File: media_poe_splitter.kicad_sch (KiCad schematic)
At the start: 30 parts, among them J1 Screw_Terminal_01x02, X1 7499811120

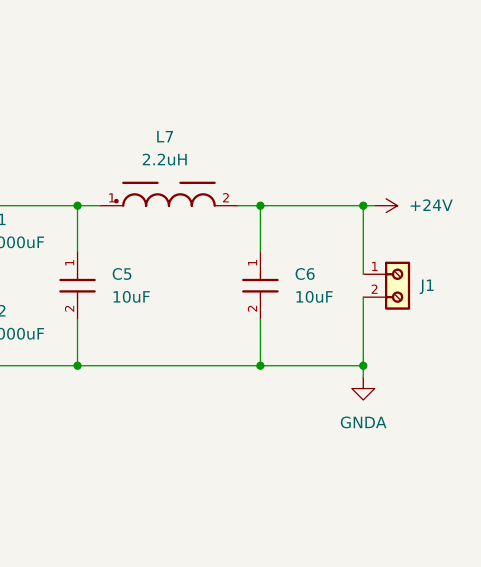
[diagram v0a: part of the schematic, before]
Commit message: poe: add missing tracks
Signed-off-by: Marc 'risson' Schmitt <marc.schmitt@risson.space>
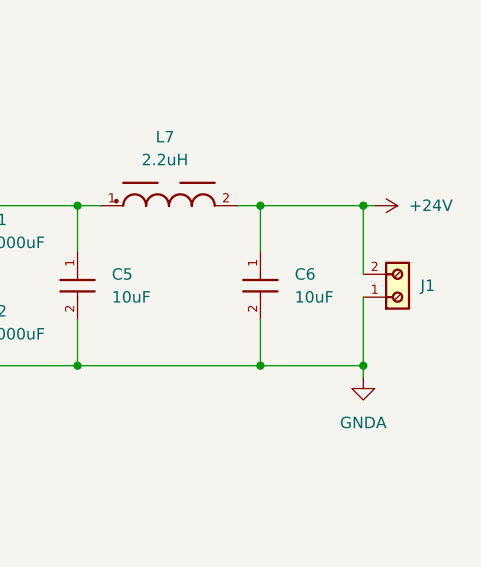
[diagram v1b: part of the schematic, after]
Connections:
- net +24V: now also J1.2; no longer J1.1
- net GNDA: now also J1.1; no longer J1.2
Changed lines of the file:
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@@
 	(symbol
 		(lib_id "691210910002:691210910002")
-		(at 415.29 382.27 270)
+		(at 415.29 379.73 270)
+		(mirror x)
 		(unit 1)
 		(exclude_from_sim no)
@@
 		(on_board yes)
 		(dnp no)
-		(fields_autoplaced yes)
 		(property "Reference" "J1"
-			(at 416.56 380.9999 90)
+			(at 416.56 381.0001 90)
 			(effects
 				(font
@@
 		)
 		(property "Value" "Screw_Terminal_01x02"
-			(at 412.7501 384.81 0)
+			(at 412.7501 377.19 0)
 			(effects
 				(font
@@
 		)
 		(property "Footprint" "691210910002:691210910002"
-			(at 415.29 382.27 0)
+			(at 415.29 379.73 0)
 			(effects
 				(font
@@
 		)
 		(property "Datasheet" "https://www.we-online.com/components/products/datasheet/691210910002.pdf"
-			(at 415.29 382.27 0)
+			(at 415.29 379.73 0)
 			(effects
 				(font
@@
 		)
 		(property "Description" "WR-TBL Series 2109 - Rising Cage Clamp - THT - 2.54mm"
-			(at 415.29 382.27 0)
+			(at 415.29 379.73 0)
 			(effects
 				(font
@@
 		)
 		(property "Mount" "THT"
-			(at 415.29 382.27 0)
+			(at 415.29 379.73 0)
 			(effects
 				(font
@@
 		)
 		(property "MPN" "691210910002"
-			(at 415.29 382.27 0)
+			(at 415.29 379.73 0)
 			(effects
 				(font
@@
 		)
 		(property "Manufacturer" "Wurth Elektronik"
-			(at 415.29 382.27 0)
+			(at 415.29 379.73 0)
 			(effects
 				(font
@@
 		)
 		(property "Manufactuer" ""
-			(at 415.29 382.27 0)
+			(at 415.29 379.73 0)
 			(effects
 				(font

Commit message: add USB controller, finish board
Signed-off-by: Marc 'risson' Schmitt <marc.schmitt@risson.space>
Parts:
- removed C5, C6: 10uF, 885012209073:885012209073, symbol 885012209073:885012209073
- removed L7: 2.2uH, 744774022:744774022, symbol 744774022:744774022
- added C10, C11, C12, C13, C18, C20, C23, C24, C25, C26, C27, C28, C29, C30, C31, C32, C5, C6, C7: 100nF 25V, 885012206071:885012206071, symbol 885012206071:885012206071
- added C14, C15, C19: 1uF 16V, 885012206052:885012206052, symbol 885012206052:885012206052
- added C16, C3: 15pF 50V, 885012005056:885012005056, symbol 885012005056:885012005056
- added C17, C33: 10uF 6.3V, 885012207003:885012207003, symbol 885012207003:885012207003
- added C4: 2.2uF 25V, 885012207079:885012207079, symbol 885012207079:885012207079
- added C8: 10nF 6.3V, 885012104004:885012104004, symbol 885012104004:885012104004
- added D10, D11: 5Vdc, 824014885:824014885, symbol 824014885:824014885
- added D13: 824012823, 824012823:824012823, symbol 824012823:824012823
- added IC1: LAN7850-I_8JX, LAN7850-I_8JX:LAN7850-I_8JX, symbol LAN7850-I_8JX:LAN7850-I_8JX
- added IC2: 17791063215, 17791063215:17791063215, symbol 17791063215:17791063215
- added IC3: 93AA66C-I/SN, 93AA66C-I_SN:93AA66C-I_SN, symbol 93AA66C-I_SN:93AA66C-I_SN
- added L7: 744232090, 744232090:744232090, symbol 744232090:744232090
- added L9: VLF302515MT-3R3M, VLF302515MT-3R3M:VLF302515MT-3R3M, symbol VLF302515MT-3R3M:VLF302515MT-3R3M
- added R1, R3, R4, R7: 10K, RC0603FR-0710KL:RC0603FR-0710KL, symbol RC0603FR-0710KL:RC0603FR-0710KL
- added R10: 12K, RC0603FR-0712KL:RC0603FR-0712KL, symbol RC0603FR-0712KL:RC0603FR-0712KL
- added R11, R2: 330R, RC0603FR-07340RL:RC0603FR-07340RL, symbol RC0603FR-07340RL:RC0603FR-07340RL
- added R6: 47.8K, RC0603FR-0748K7L:RC0603FR-0748K7L, symbol RC0603FR-0748K7L:RC0603FR-0748K7L
- added R8: 2K, RC0603FR-072KL:RC0603FR-072KL, symbol RC0603FR-072KL:RC0603FR-072KL
- added R9: 100K, RC0603FR-07100KL:RC0603FR-07100KL, symbol RC0603FR-07100KL:RC0603FR-07100KL
- added S1: 435151014824, 435151014824:435151014824, symbol 435151014824:435151014824
- added X2: 68710614522, 68710614522:68710614522, symbol 68710614522:68710614522
- added Y1: 830055299, 830055299:830055299, symbol 830055299:830055299
- C101, C21, C22, D1, D2, D3, D4, D5, D6, D7, D8, D9, R101, R102, R103, R104: Mount SMD -> SMT
- L1, L2, L3, L4, L5, L6: Manufacturer Wurth Electronics -> Wurth Elektronik; Mount SMD -> SMT
- X1: Manufacturer Würth Elektronik -> Wurth Elektronik
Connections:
- net +24V: now also B1.10 (VOUT2), B1.9 (VOUT2), C1.1, C4.1, C7.1, IC2.2 (+VIN)
- net GNDA: now also C4.2, C7.2, IC2.1 (-VIN)
- net GNDPWR: now also C13.2, C6.2, R11.2, R2.2, S1.5, S1.6, X2.6, X2.Z1, X2.Z2
- net TR3_P: now reaches X1.11 (TRD4+)
- net TR3_P: now also D11.6, IC1.10 (TR3P)
- net TR3_N: now reaches X1.12 (TRD4-)
- net TR3_N: now also D11.5, IC1.11 (TR3N)
- net TR1_P: now reaches X1.2 (TRD2+)
- net TR1_P: now also D10.6, IC1.4 (TR1P)
- net TR1_N: now reaches X1.3 (TRD2-)
- net TR1_N: now also D10.5, IC1.5 (TR1N)
- net TR2_P: now reaches X1.4 (TRD3+)
- net TR2_P: now also D11.1, IC1.7 (TR2P)
- net TR2_N: now reaches X1.5 (TRD3-)
- net TR2_N: now also D11.9, IC1.8 (TR2N)
- net TR0_P: now reaches X1.7 (TRD1+)
- net TR0_P: now also D10.1, IC1.1 (TR0P)
- net TR0_N: now reaches X1.8 (TRD1-)
- net TR0_N: now also D10.9, IC1.2 (TR0N)
- new net: IC1.18 (VDD12_SW_OUT), L9.1
- new net: C3.1, IC1.46 (XI), Y1.1
- new net: C16.1, IC1.47 (XO), Y1.3
- new net: IC1.21 (EECS/GPIO1), IC3.1 (CS), R7.1
- new net: IC1.22 (EEDI/GPIO2), IC3.3 (DI)
- new net: IC1.23 (EEDO/GPIO3), IC3.4 (DO)
- new net: IC1.24 (EECLK/GPIO4), IC3.2 (CLK)
- new net: IC1.27 (VBUS_DET), R4.1
- new net: IC1.40 (TEST), R1.1
- new net: IC1.43 (USBRBIAS), R10.1
- new net: IC1.55 (REF_REXT), R8.1
- new net: C19.2, IC1.56 (REF_FILT)
- new net: IC3.6 (ORG), R3.1
- new net: D13.2, L7.1, X2.3
- new net: D13.1, L7.4, X2.2
- new net: IC2.8 (FB), R6.1
- new net +1V2: C11.2, C12.1, C17.1, C18.1, C20.1, C23.1, C24.1, IC1.20 (VDD12_SW_FB), IC1.26 (VDD12CORE), IC1.33 (VDD12A), IC1.34 (VDD12HSIC), IC1.48 (VDD12CORE), IC1.52 (VDD12A), L9.2
- new net +2V5: C14.1, C25.1, C26.1, C27.1, C28.1, IC1.12 (VDD25A), IC1.3 (VDD25A), IC1.53 (VDD25_REG_OUT), IC1.6 (VDD25A), IC1.9 (VDD25A)
- new net +3V3: C10.1, C15.1, C29.1, C30.1, C31.1, C32.1, C33.1, C5.2, C8.1, IC1.13 (VDDVARIO), IC1.19 (VDD_SW_IN), IC1.25 (VDDVARIO), IC1.42 (VDDVARIO), IC1.44 (VDD33A), IC1.45 (VDDVARIO), IC1.54 (VDD33_REG_IN), IC2.6 (+VOUT), IC3.8 (VCC), R4.2, R9.2
- new net GND: C10.2, C11.1, C12.2, C13.1, C14.2, C15.2, C16.2, C17.2, C18.2, C19.1, C20.2, C23.2, C24.2, C25.2, C26.2, C27.2, C28.2, C29.2, C3.2, C30.2, C31.2, C32.2, C33.2, C5.1, C6.1, C8.2, D10.3, D11.3, D13.3, IC1.30 (HSIC_SEL), IC1.57 (VSS), IC2.7 (-VOUT), IC3.5 (VSS), R1.2, R10.2, R11.1, R2.1, R3.2, R6.2, R7.2, R8.2, S1.3, S1.4, X2.5, Y1.2, Y1.4
- new net LED0: IC1.31 (LED0/GPIO7)
- new net LED2: IC1.50 (LED2/GPIO10)
- new net RESET_N: IC1.41 (RESET_N/PME_CLEAR), R9.1, S1.1, S1.2
- new net USBD_M: IC1.37 (USB_DM), L7.3
- new net USBD_P: IC1.36 (USB_DP), L7.2
- no-connect marks 11 -> 39
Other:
- moved on the sheet: C101, J1

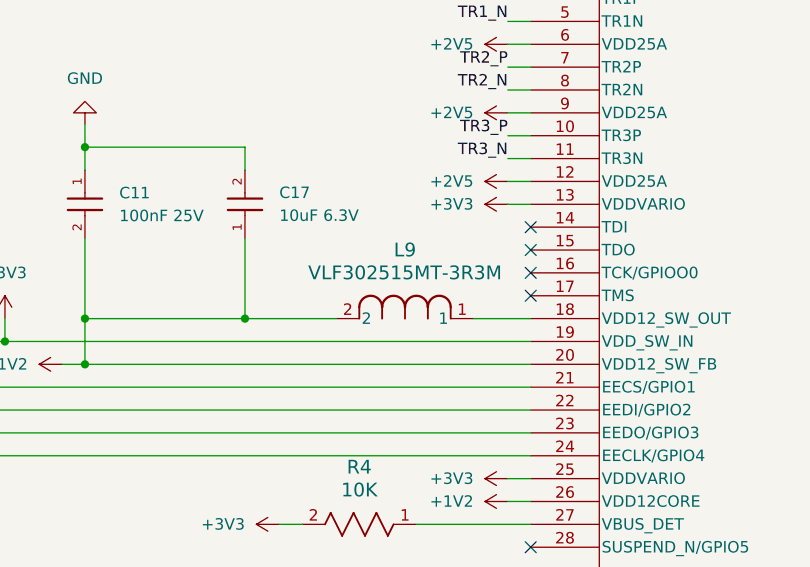
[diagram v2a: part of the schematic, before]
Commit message: replace NLA part
Signed-off-by: Marc 'risson' Schmitt <marc.schmitt@risson.space>
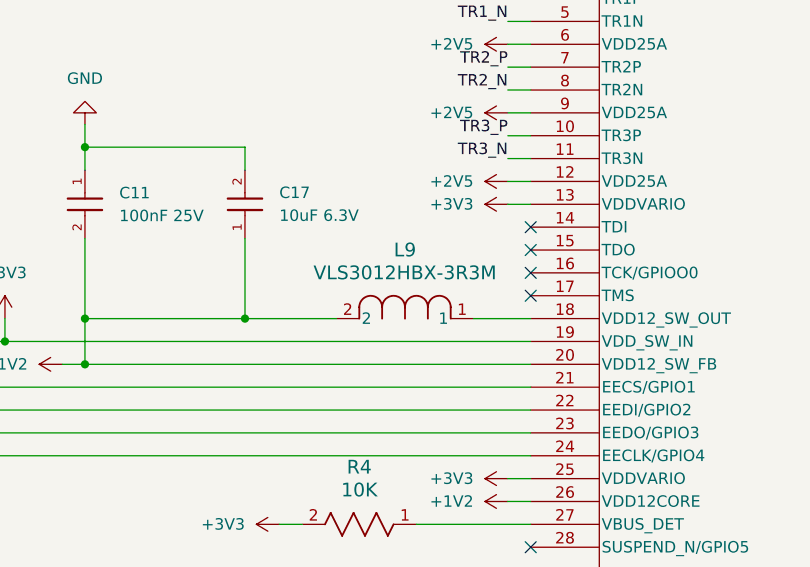
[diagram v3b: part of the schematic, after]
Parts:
- removed L9: VLF302515MT-3R3M, VLF302515MT-3R3M:VLF302515MT-3R3M, symbol VLF302515MT-3R3M:VLF302515MT-3R3M
- added L9: VLS3012HBX-3R3M, VLS3012HBX-3R3M:VLS3012HBX-3R3M, symbol VLS3012HBX-3R3M:VLS3012HBX-3R3M
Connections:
- net +1V2: now also L9.2
- net at IC1.18 (VDD12_SW_OUT): now also L9.1
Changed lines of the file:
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@@
 	)
 	(symbol
-		(lib_id "VLF302515MT-3R3M:VLF302515MT-3R3M")
-		(at 269.24 157.48 0)
-		(unit 1)
-		(exclude_from_sim no)
-		(in_bom yes)
-		(on_board yes)
-		(dnp no)
-		(fields_autoplaced yes)
-		(property "Reference" "L9"
-			(at 276.86 149.86 0)
-			(effects
-				(font
-					(size 1.524 1.524)
-				)
-			)
-		)
-		(property "Value" "VLF302515MT-3R3M"
-			(at 276.86 152.4 0)
-			(effects
-				(font
-					(size 1.524 1.524)
-				)
-			)
-		)
-		(property "Footprint" "VLF302515MT-3R3M:VLF302515MT-3R3M"
-			(at 269.24 157.48 0)
-			(effects
-				(font
-					(size 1.27 1.27)
-					(italic yes)
-				)
-				(hide yes)
-			)
-		)
-		(property "Datasheet" "https://mm.digikey.com/Volume0/opasdata/d220001/medias/docus/2218/VLF302515MT_Series.pdf"
-			(at 269.24 157.48 0)
-			(effects
-				(font
-					(size 1.27 1.27)
-					(italic yes)
-				)
-				(hide yes)
-			)
-		)
-		(property "Description" "FIXED IND 3.3UH 2.25A 72MOHM SMD"
-			(at 269.24 157.48 0)
-			(effects
-				(font
-					(size 1.27 1.27)
-				)
-				(hide yes)
-			)
-		)
-		(property "Manufacturer" "TDK Corporation"
-			(at 269.24 157.48 0)
-			(effects
-				(font
-					(size 1.27 1.27)
-				)
-				(hide yes)
-			)
-		)
-		(property "Mount" "SMT"
-			(at 269.24 157.48 0)
-			(effects
-				(font
-					(size 1.27 1.27)
-				)
-				(hide yes)
-			)
-		)
-		(property "MPN" "VLF302515MT-3R3M"
-			(at 269.24 157.48 0)
-			(effects
-				(font
-					(size 1.27 1.27)
-				)
-				(hide yes)
-			)
-		)
-		(pin "2"
-		)
-		(pin "1"
-		)
-		(instances
-			(project ""
-				(path "/6322d6ab-712b-4593-ad2b-135ce593cd38"
-					(reference "L9")
-					(unit 1)
-				)
-			)
-		)
-	)
-	(symbol
 		(lib_id "power:+3V3")
 		(at 447.04 121.92 270)
@@
 					(unit 1)
 				)
+			)
+		)
+	)
+	(symbol
+		(lib_id "VLS3012HBX-3R3M:VLS3012HBX-3R3M")
+		(at 269.24 157.48 0)
+		(unit 1)
+		(exclude_from_sim no)
+		(in_bom yes)
+		(on_board yes)
+		(dnp no)
+		(fields_autoplaced yes)
+		(property "Reference" "L9"
+			(at 276.86 149.86 0)
+			(effects
+				(font
+					(size 1.524 1.524)
+				)
+			)
+		)
+		(property "Value" "VLS3012HBX-3R3M"
+			(at 276.86 152.4 0)
+			(effects
+				(font
+					(size 1.524 1.524)
+				)
+			)
+		)
+		(property "Footprint" "VLS3012HBX-3R3M:VLS3012HBX-3R3M"
+			(at 269.24 157.48 0)
+			(effects
+				(font
+					(size 1.27 1.27)
+					(italic yes)
+				)
+				(hide yes)
+			)
+		)
+		(property "Datasheet" "https://product.tdk.com/en/system/files/dam/doc/product/inductor/inductor/smd/catalog/inductor_commercial_power_vls3012hbx_en.pdf"
+			(at 269.24 157.48 0)
+			(effects
+				(font
+					(size 1.27 1.27)
+					(italic yes)
+				)
+				(hide yes)
+			)
+		)
+		(property "Description" "FIXED IND 3.3UH 2.63A 150MOHM SM"
+			(at 269.24 157.48 0)
+			(effects
+				(font
+					(size 1.27 1.27)
+				)
+				(hide yes)
+			)
+		)
+		(property "MPN" "VLS3012HBX-3R3M"
+			(at 269.24 157.48 0)
+			(effects
+				(font
+					(size 1.27 1.27)
+				)
+				(hide yes)
+			)
+		)
+		(property "Mount" "SMT"
+			(at 269.24 157.48 0)
+			(effects
+				(font
+					(size 1.27 1.27)
+				)
+				(hide yes)
+			)
+		)
+		(property "Manufacturer" "TDK Corporation"
+			(at 269.24 157.48 0)
+			(effects
+				(font
+					(size 1.27 1.27)
+				)
+				(hide yes)
+			)
+		)
+		(pin "2"
+		)
+		(pin "1"
+		)
+		(instances
+			(project ""
+				(path "/6322d6ab-712b-4593-ad2b-135ce593cd38"
+					(reference "L9")
+					(unit 1)
+				)

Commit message: schematic: cleanup
Signed-off-by: Marc 'risson' Schmitt <marc.schmitt@risson.space>
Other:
- note added: "24V -> 3.3V"
- note added: "Data + power input, PoE+ to PoE++ (class 4 to 8)"
- note added: "Ethernet 8 pairs -> USB"
- note added: "PoE processing + 24V output"
- note added: "Power filtering"
- note added: "Reset switch for USB controller"
- note added: "USB output (via flex cable)"
- company: (none) -> Marc 'risson' Schmitt
- title: (none) -> PoE splitter to 24V + USB
- moved on the sheet: B1, C1, C10, C101, C11, C12, C13, C14, C15, C16, C17, C18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
